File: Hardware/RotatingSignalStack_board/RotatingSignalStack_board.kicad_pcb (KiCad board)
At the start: 2 copper layers, 69.1 x 69 mm, 32 parts, among them J1 8P8C_LED_Shielded, J2 Conn_01x05_Pin, SW1 SW_Push, SW2 SW_Push, U1 OKI, U3 Teensy4.1_DEV-16771

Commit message: Minor layout changes
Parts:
- R5: footprint Jumper:SolderJumper-2_P1.3mm_Open_RoundedPad1.0x1.5mm -> Resistor_SMD:R_0603_1608Metric_Pad0.98x0.95mm_HandSolder
- moved C3 10.6 mm to (132.6, 137.9), turned to 0 degrees
- moved C4 9.87 mm to (132.6, 140.0), turned to 0 degrees
- moved C5 9.78 mm to (132.6, 142.0), turned to 0 degrees
- moved C2 2.41 mm to (135.9, 134.1), turned to -90 degrees
- moved R5 1.21 mm to (150.9, 103.9)
- moved C1 0.98 mm to (144.5, 134.1)
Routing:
- net JOG B: track 46.5 -> 63.8 mm
- net JOG A: track 46.1 -> 57.8 mm
- net /Rx-: track 55.4 -> 43.7 mm
- net /Rx+: track 55.4 -> 43.8 mm
- net +12V: track 42.5 -> 46.7 mm, vias 0 -> 1
- net +3.3V: track 167.9 -> 171.2 mm, vias 3 -> 4
- net MAG ENABLE: track 59.2 -> 58.4 mm
- net GND: vias 14 -> 15
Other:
- board text added: "HBRIDGE"
- board text added: "Signal Stack Board, Rev1 Mars Rover Design Team Missouri S&T, 2024 Tyler Lunyou"
- board text removed: "H.BRIDGE"
- board text removed: "SIGNAL STACK BOARD - REV1 MARS ROVER DESIGN TEAM MISSORUI S&T - 2024 TYLER LUNYOU"

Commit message: Redid layout
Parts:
- removed Conn6: Molex_SL_05, MRDT_Connectors:MOLEX_SL_05_Vertical
- removed D13, D14: Blue, LED_SMD:LED_0603_1608Metric_Pad1.05x0.95mm_HandSolder
- removed the G*** at (151.2, 87.1)
- removed J2: Conn_01x05_Pin, Connector_PinHeader_2.54mm:PinHeader_1x05_P2.54mm_Vertical
- removed R13, R18: 100, Resistor_SMD:R_0603_1608Metric_Pad0.98x0.95mm_HandSolder
- removed U3: Teensy4.1_DEV-16771, MRDT_Shields:Teensy_4_1_Ethernet
- added Conn4: Molex_SL_03, MRDT_Connectors:MOLEX_SL_03_Horizontal, F.Cu at (136.7, 99.9)
- added D3: Blue, LED_SMD:LED_0603_1608Metric_Pad1.05x0.95mm_HandSolder, F.Cu at (188.7, 104.1)
- added D4: Blue, LED_SMD:LED_0603_1608Metric_Pad1.05x0.95mm_HandSolder, F.Cu at (188.7, 93.5)
- added G***: LOGO, MRDT_Silkscreens:0_MRDT_Logo_10mm, F.Cu at (193.3, 82.0)
- added G***: LOGO, MRDT_Silkscreens:z_sig_Grant_Brinker_25mmx6, B.Cu at (180.3, 74.9)
- added G***: LOGO, MRDT_Silkscreens:yagi, B.Cu at (133.9, 89.4)
- added G***: LOGO, MRDT_Silkscreens:0_MRDT_Logo_10mm, B.Cu at (128.3, 77.5)
- added R6: 100, Resistor_SMD:R_0603_1608Metric_Pad0.98x0.95mm_HandSolder, F.Cu at (188.7, 109.4)
- added R7: 100, Resistor_SMD:R_0603_1608Metric_Pad0.98x0.95mm_HandSolder, F.Cu at (188.7, 98.7)
- added U2: Teensy4.1_DEV-16771, MRDT_Shields:Teensy_4_1_Ethernet, F.Cu at (155.7, 77.2)
- C1: value 10uF -> 0.1uF
- C3: value 0.1uF -> 10uF
- C4: value 10uF -> 22uF
- C5: value 22uF -> 10uF
- Conn1: value Molex_SL_03 -> AndersonPP; footprint MRDT_Connectors:MOLEX_SL_03_Vertical -> MRDT_Connectors:Square_Anderson_2_H_Stacked
- Conn2: footprint MRDT_Connectors:Square_Anderson_2_H_Side_By_Side -> MRDT_Connectors:Square_Anderson_2_H_Stacked
- Conn3: value AndersonPP -> Molex_SL_05; footprint MRDT_Connectors:Square_Anderson_2_H_Side_By_Side -> MRDT_Connectors:MOLEX_SL_05_Horizontal
- R1: value 100 -> 1k
- R2: value 1k -> 100
- R3: value 4.7k -> 0
- R5: value 0 -> 4.7k; moved to F.Cu
- moved V3 97.7 mm to (105.1, 75.1), turned to 90 degrees
- moved C5 76.5 mm to (108.7, 69.3)
- moved Conn1 73.1 mm to (108.9, 94.6), turned to 90 degrees
- moved V2 72.4 mm to (191.1, 75.1), turned to 0 degrees
- moved D2 69.2 mm to (103.5, 85.9)
- moved R2 65.7 mm to (103.6, 88.1)
- moved R4 63.7 mm to (146.6, 88.4), turned to 0 degrees
- moved C2 63.1 mm to (104.9, 79.1), turned to 90 degrees
- moved U1 62.9 mm to (107.8, 78.2), turned to 90 degrees
- moved C4 57.4 mm to (103.6, 90.4), turned to 180 degrees
- moved C1 56.6 mm to (103.6, 95.0), turned to 180 degrees
- moved R1 55.3 mm to (103.6, 97.0)
- moved D1 55.2 mm to (103.6, 99.1)
- moved C3 53.7 mm to (103.6, 92.7), turned to 180 degrees
- moved R3 49.2 mm to (158.8, 96.5), turned to 180 degrees
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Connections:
- C2 pad 1: +3.3V -> +12V
- C5 pad 1: +12V -> +3.3V
- Conn1 pad 1: HB_FWD -> GND
- Conn3 pad 1: GND -> MAG ENABLE
- Conn3 pad 2: +12V -> I2C SDA
- R1 pad 1: +3.3V -> Net-(D1-A)
- R1 pad 2: Net-(D1-A) -> +12V
- R2 pad 1: Net-(D2-A) -> +3.3V
- R2 pad 2: +12V -> Net-(D2-A)
- R3 pad 1: COMP PWR -> +3.3V
- R3 pad 2: I2C SDA -> MAG ENABLE
- R4 pad 2: I2C SCL -> I2C SDA
- R5 pad 1: +3.3V -> COMP PWR
- R5 pad 2: MAG ENABLE -> I2C SCL
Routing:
- net +3.3V: track 171.2 -> 266.8 mm, vias 4 -> 1
- net COMP PWR: track 78.4 -> 19.4 mm, vias 2 -> 0
- net I2C SCL: track 70.8 -> 23.2 mm, vias 4 -> 0
- net I2C SDA: track 64.0 -> 26.7 mm, vias 3 -> 2
- net MAG ENABLE: track 58.4 -> 21.5 mm, vias 1 -> 0
- net HB_FWD: track 48.8 -> 15.1 mm, vias 1 -> 0
- net /Tx+: track 55.8 -> 22.5 mm
- net /Tx-: track 55.8 -> 23.0 mm
- net /LED: track 64.6 -> 32.3 mm
- net HB_RVS: track 47.3 -> 15.1 mm, vias 1 -> 0
- net /Rx+: track 43.8 -> 15.6 mm
- net /Rx-: track 43.7 -> 15.8 mm
- net JOG B: track 63.8 -> 37.7 mm, vias 1 -> 0
- net JOG A: track 57.8 -> 51.0 mm, vias 1 -> 0
- net Net-(D4-A): track 0.00 -> 3.44 mm
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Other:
- board size 69.1 x 69 mm -> 102 x 46.2 mm
- board text added: "3V3"
- board text added: "Compass"
- board text added: "ENB"
- board text added: "FWD"
- board text added: "GND"
- board text added: "H-Bridge"
- board text added: "RVS"
- board text added: "SCL"
- board text added: "SDA"
- board text added: "Signal Stack Board, Rev1 Mars Rover Design Team Missouri S&T, 2024 Grant Brinker"
- board text removed: "12v"
- board text removed: "3.3v"
- board text removed: "3.3v Direct Power Compass"
- board text removed: "COMPASS"
- board text removed: "HBRIDGE"
- board text removed: "IN"
- board text removed: "L"
- board text removed: "OUT"
- board text removed: "R"
- board text removed: "Signal Stack Board, Rev1 Mars Rover Design Team Missouri S&T, 2024 Tyler Lunyou"

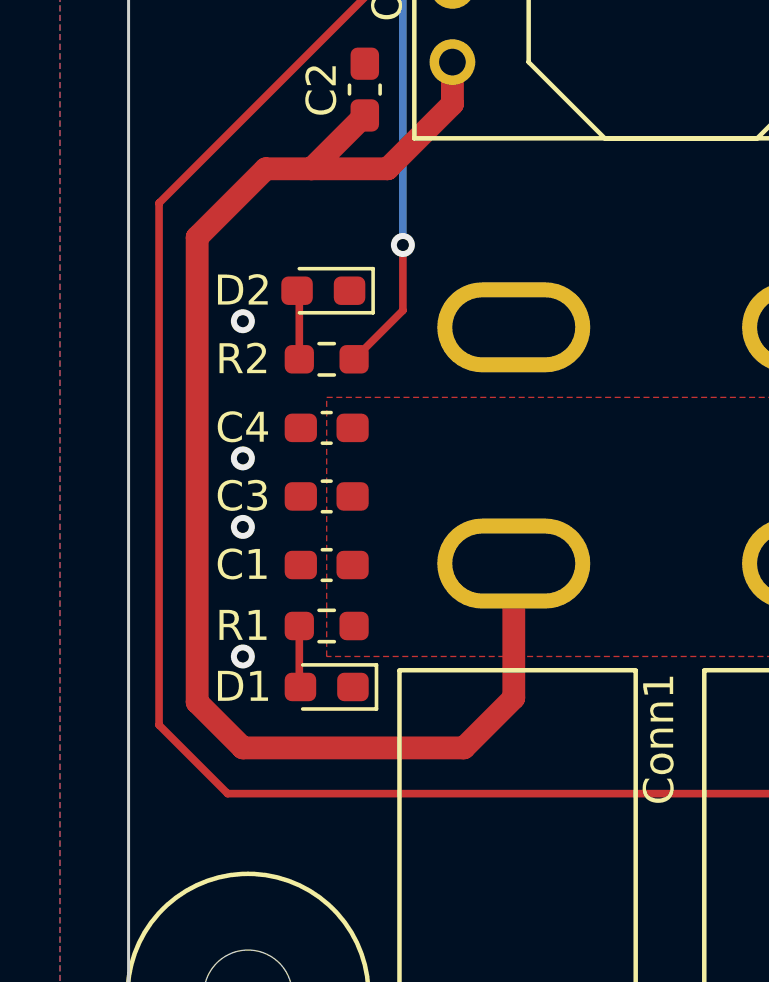
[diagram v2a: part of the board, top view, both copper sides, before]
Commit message: Added LED labels
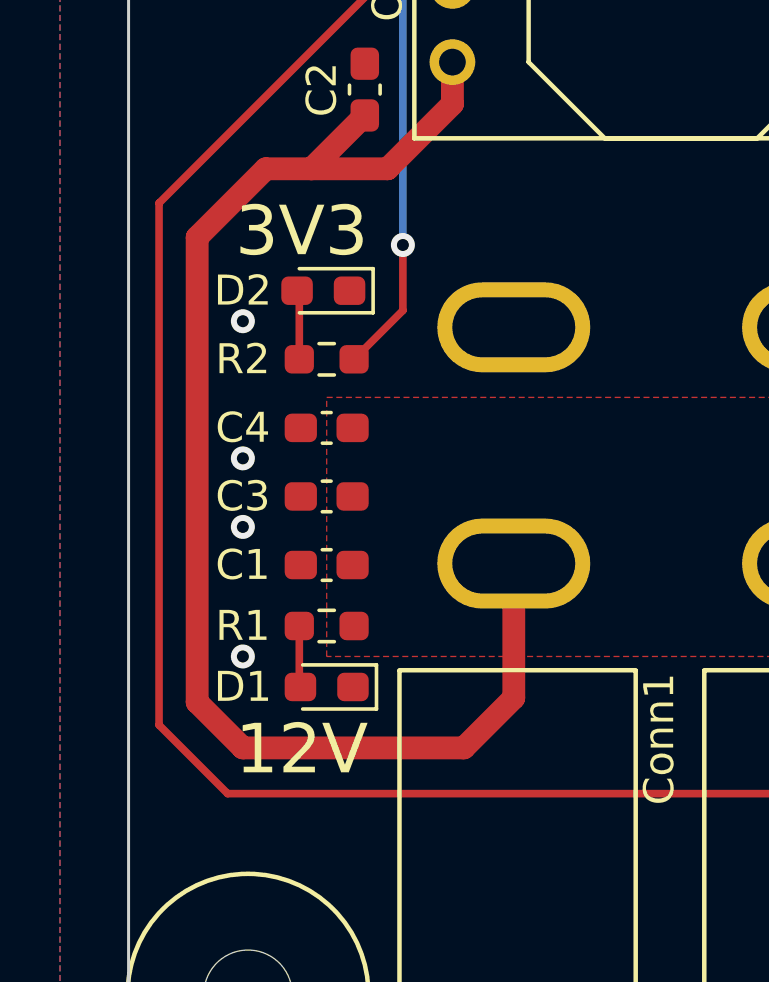
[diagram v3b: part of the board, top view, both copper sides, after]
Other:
- board text added: "12V"
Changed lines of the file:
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@@
     (effects (font (size 1.27 1.27) (thickness 0.15)) (justify left bottom))
+  )
+  (gr_text "3V3" (at 100.584 84.836) (layer "F.SilkS")
+    (effects (font (size 1.651 1.651) (thickness 0.15)) (justify left bottom))
   )
   (gr_text "H-Bridge" (at 134.112 93.98) (layer "F.SilkS")
     (effects (font (size 1.651 1.651) (thickness 0.3302) bold) (justify bottom))
   )
+  (gr_text "12V" (at 100.584 102.108) (layer "F.SilkS")
+    (effects (font (size 1.651 1.651) (thickness 0.15)) (justify left bottom))
+  )
   (gr_text "ENB" (at 156.464 98.298 90) (layer "F.SilkS")
